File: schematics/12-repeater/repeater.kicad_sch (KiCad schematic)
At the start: 9 parts, among them J13 PSG01571, J5 RJHSE-5380, U6 PCA9600D

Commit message: Move schematics to correct folders
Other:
- title: PROJECT ROYALE INSTRUMENTATION -> PROJECT ROYALE REPEATER
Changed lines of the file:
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@@
   (paper "A4")
   (title_block
-    (title "PROJECT ROYALE INSTRUMENTATION")
-    (date "2021-11-26")
+    (title "PROJECT ROYALE REPEATER")
+    (date "2022-02-08")
     (rev "2.1")
     (company "Cambridge University Spaceflight")
@@
     (effects (font (size 1.27 1.27)) (justify right))
   )
-  (symbol (lib_id "royale:PCA9600D") (at 130.81 99.06 0)
+  (symbol (lib_id "royale:PCA9600D") (at 130.81 99.06 0) (unit 1)
     (in_bom yes) (on_board yes)
     (property "Reference" "U6" (id 0) (at 132.08 87.63 0)
@@
     (pin "8")
   )
-  (symbol (lib_id "royale:R") (at 111.76 91.44 270)
+  (symbol (lib_id "royale:R") (at 111.76 91.44 270) (unit 1)
     (in_bom yes) (on_board yes)
     (property "Reference" "R25" (id 0) (at 113.03 91.44 90)
@@
     (pin "2")
   )
-  (symbol (lib_id "royale:R") (at 104.14 91.44 270)
+  (symbol (lib_id "royale:R") (at 104.14 91.44 270) (unit 1)
     (in_bom yes) (on_board yes)
     (property "Reference" "R24" (id 0) (at 105.41 91.44 90)
@@
     (pin "2")
   )
-  (symbol (lib_id "royale:R") (at 146.05 88.9 270)
+  (symbol (lib_id "royale:R") (at 146.05 88.9 270) (unit 1)
     (in_bom yes) (on_board yes)
     (property "Reference" "R26" (id 0) (at 147.32 88.9 90)
@@
     (pin "2")
   )
-  (symbol (lib_id "royale:R") (at 161.29 88.9 270)
+  (symbol (lib_id "royale:R") (at 161.29 88.9 270) (unit 1)
     (in_bom yes) (on_board yes)
     (property "Reference" "R27" (id 0) (at 162.56 88.9 90)
@@
     (pin "2")
   )
-  (symbol (lib_id "royale:12v") (at 130.81 82.55 0)
+  (symbol (lib_id "royale:12v") (at 130.81 82.55 0) (unit 1)
     (in_bom yes) (on_board yes)
     (property "Reference" "#PWR028" (id 0) (at 130.81 79.756 0)
@@
     (pin "1")
   )
-  (symbol (lib_id "cusf-kicad:GND") (at 130.81 114.3 0)
+  (symbol (lib_id "cusf-kicad:GND") (at 130.81 114.3 0) (unit 1)
     (in_bom yes) (on_board yes)
     (property "Reference" "#PWR029" (id 0) (at 127.508 113.284 0)
@@
     (pin "1")
   )
-  (symbol (lib_id "royale:GND") (at 203.2 104.14 0)
+  (symbol (lib_id "royale:GND") (at 203.2 104.14 0) (unit 1)
     (in_bom yes) (on_board yes)
     (property "Reference" "#PWR051" (id 0) (at 199.898 103.124 0)
@@
     (pin "1")
   )
-  (symbol (lib_id "royale:GND") (at 185.42 104.14 0)
+  (symbol (lib_id "royale:GND") (at 185.42 104.14 0) (unit 1)
     (in_bom yes) (on_board yes)
     (property "Reference" "#PWR049" (id 0) (at 182.118 103.124 0)
@@
     (pin "1")
   )
-  (symbol (lib_id "royale:Conn_02x04") (at 193.04 96.52 0)
+  (symbol (lib_id "royale:Conn_02x04") (at 193.04 96.52 0) (unit 1)
     (in_bom yes) (on_board yes)
     (property "Reference" "J5" (id 0) (at 194.31 87.63 0))
@@
     (pin "8")
   )
-  (symbol (lib_id "royale:3v3") (at 104.14 82.55 0)
+  (symbol (lib_id "royale:3v3") (at 104.14 82.55 0) (unit 1)
     (in_bom yes) (on_board yes)
     (property "Reference" "#PWR027" (id 0) (at 104.14 79.756 0)
@@
     (pin "1")
   )
-  (symbol (lib_id "royale:C") (at 173.99 106.68 90) (mirror x)
+  (symbol (lib_id "royale:C") (at 173.99 106.68 90) (mirror x) (unit 1)
     (in_bom yes) (on_board yes)
     (property "Reference" "C17" (id 0) (at 172.72 106.68 90)
@@
     (pin "2")
   )
-  (symbol (lib_id "royale:12v") (at 185.42 91.44 0)
+  (symbol (lib_id "royale:12v") (at 185.42 91.44 0) (unit 1)
     (in_bom yes) (on_board yes)
     (property "Reference" "#PWR048" (id 0) (at 185.42 88.646 0)
@@
     (pin "1")
   )
-  (symbol (lib_id "royale:12v") (at 203.2 91.44 0)
+  (symbol (lib_id "royale:12v") (at 203.2 91.44 0) (unit 1)
     (in_bom yes) (on_board yes)
     (property "Reference" "#PWR050" (id 0) (at 203.2 88.646 0)
@@
     (pin "1")
   )
-  (symbol (lib_id "Diode:BAT54A") (at 151.13 106.68 0)
+  (symbol (lib_id "Diode:BAT54A") (at 151.13 106.68 0) (unit 1)
     (in_bom yes) (on_board yes) (fields_autoplaced)
     (property "Reference" "D2" (id 0) (at 151.13 100.33 0))
@@
     (pin "3")
   )
-  (symbol (lib_id "Connector:Mini-DIN-4") (at 81.28 111.76 0)
+  (symbol (lib_id "Connector:Mini-DIN-4") (at 81.28 111.76 0) (unit 1)
     (in_bom yes) (on_board yes)
     (property "Reference" "J13" (id 0) (at 88.9 105.41 0))
@@
     (pin "4")
   )
-  (symbol (lib_id "cusf-kicad:GND") (at 90.17 113.03 0)
+  (symbol (lib_id "cusf-kicad:GND") (at 90.17 113.03 0) (unit 1)
     (in_bom yes) (on_board yes)
     (property "Reference" "#PWR0103" (id 0) (at 86.868 112.014 0)
@@
     (pin "1")
   )
-  (symbol (lib_id "royale:12v") (at 73.66 115.57 180)
+  (symbol (lib_id "royale:12v") (at 73.66 115.57 180) (unit 1)
     (in_bom yes) (on_board yes)
     (property "Reference" "#PWR0104" (id 0) (at 73.66 118.364 0)
@@
     (pin "1")
   )
+  (sheet_instances
+    (path "/" (page "1"))
+  )
+  (symbol_instances
+    (path "/00000000-0000-0000-0000-000061a3f116"
+      (reference "#PWR027") (unit 1) (value "3v3") (footprint "")
+    )
+    (path "/00000000-0000-0000-0000-000061a2516b"
+      (reference "#PWR028") (unit 1) (value "12v") (footprint "")
+    )
+    (path "/00000000-0000-0000-0000-000061a2a4f9"
+      (reference "#PWR029") (unit 1) (value "GND") (footprint "")
+    )
+    (path "/00000000-0000-0000-0000-000061a8760f"
+      (reference "#PWR048") (unit 1) (value "12v") (footprint "")
+    )
+    (path "/00000000-0000-0000-0000-000061a2d2a3"
+      (reference "#PWR049") (unit 1) (value "GND") (footprint "")
+    )
+    (path "/00000000-0000-0000-0000-000061a879ee"
+      (reference "#PWR050") (unit 1) (value "12v") (footprint "")
+    )
+    (path "/00000000-0000-0000-0000-000061a2d29d"
+      (reference "#PWR051") (unit 1) (value "GND") (footprint "")
+    )
+    (path "/9d167c4c-9461-46c4-b3b1-4f3c97404f84"
+      (reference "#PWR0103") (unit 1) (value "GND") (footprint "")
+    )
+    (path "/ddaa02b0-5d92-43df-8cef-df7e364db8e9"
+      (reference "#PWR0104") (unit 1) (value "12v") (footprint "")
+    )
+    (path "/00000000-0000-0000-0000-000061a5eef5"
+      (reference "C17") (unit 1) (value "100n") (footprint "Capacitor_SMD:C_0805_2012Metric")
+    )
+    (path "/329ba30f-e553-429f-91ff-34fe3180484b"
+      (reference "D2") (unit 1) (value "BAT54A") (footprint "Package_TO_SOT_SMD:SOT-23")
+    )
+    (path "/00000000-0000-0000-0000-000061a2d2be"
+      (reference "J5") (unit 1) (value "RJHSE-5380") (footprint "Connector_RJ:RJ45_Amphenol_RJHSE5380")
+    )
+    (path "/91b1515f-01d7-467f-9976-fa4a3565e617"
+      (reference "J13") (unit 1) (value "PSG01571") (footprint "royale:Mini-Din-Through-Hole")
+    )
+    (path "/00000000-0000-0000-0000-000061a1c307"
+      (reference "R24") (unit 1) (value "4k7") (footprint "Resistor_SMD:R_0805_2012Metric")
+    )
+    (path "/00000000-0000-0000-0000-000061a1be3c"
+      (reference "R25") (unit 1) (value "4k7") (footprint "Resistor_SMD:R_0805_2012Metric")
+    )
+    (path "/00000000-0000-0000-0000-000061a1c730"
+      (reference "R26") (unit 1) (value "1k") (footprint "Resistor_SMD:R_0805_2012Metric")
+    )
+    (path "/00000000-0000-0000-0000-000061a1d18c"
+      (reference "R27") (unit 1) (value "1k") (footprint "Resistor_SMD:R_0805_2012Metric")
+    )
+    (path "/00000000-0000-0000-0000-000061a0d3e3"
+      (reference "U6") (unit 1) (value "PCA9600D") (footprint "Package_SO:SO-8_3.9x4.9mm_P1.27mm")
+    )
+  )
 )

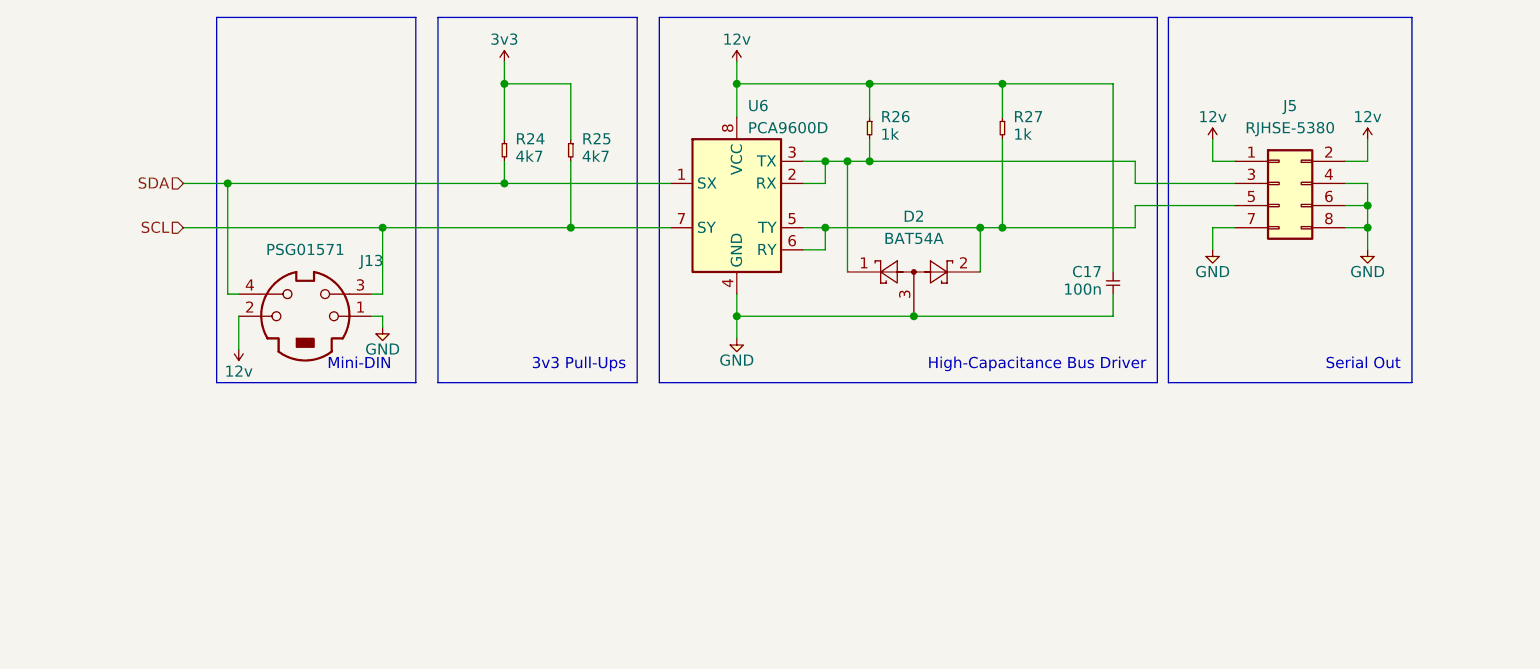
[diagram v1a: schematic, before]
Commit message: Clean up schematic and re-wire RJ45 connector
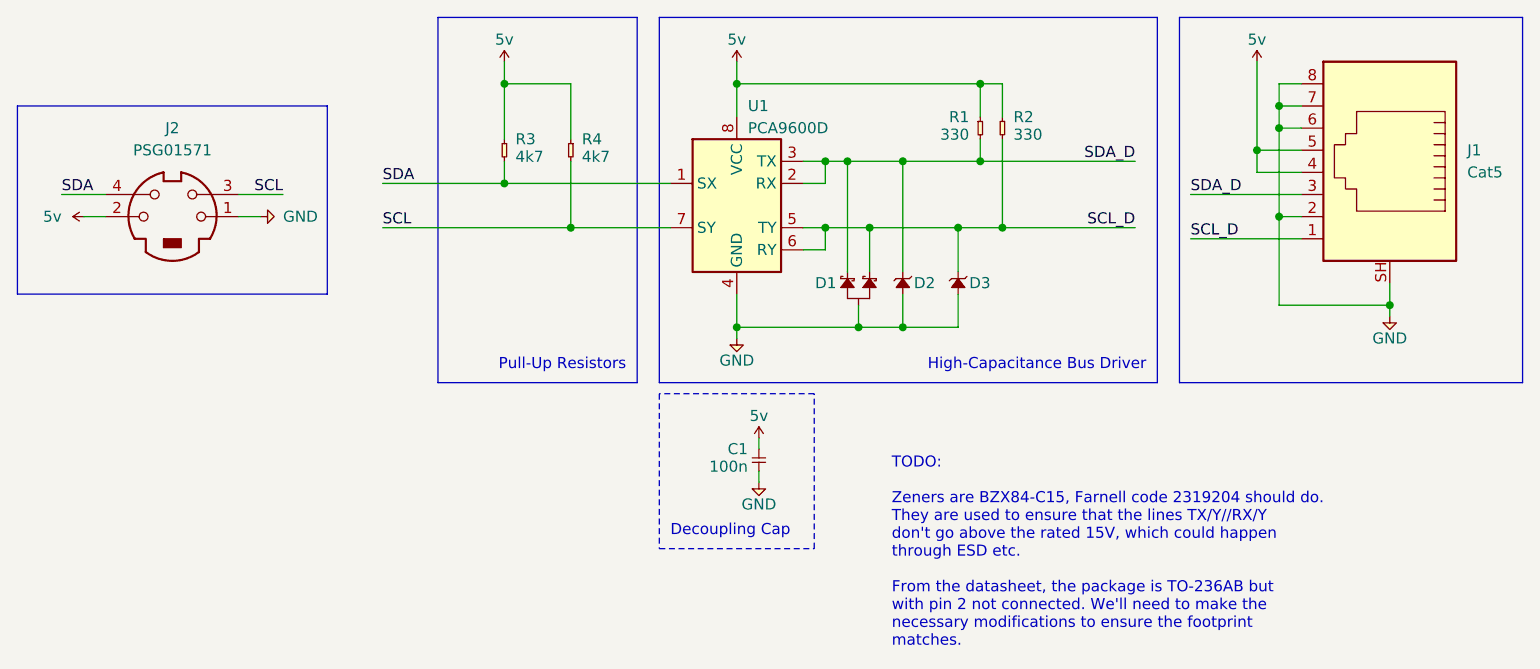
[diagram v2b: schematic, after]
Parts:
- removed D2: BAT54A, Package_TO_SOT_SMD:SOT-23, symbol Diode:BAT54A
- removed J5: RJHSE-5380, Connector_RJ:RJ45_Amphenol_RJHSE5380, symbol royale:Conn_02x04
- added D1: BAT54A, symbol royale:BAT54A
- added D2, D3: Diode_Zener, symbol royale:Diode_Zener
- added J1: Cat5, royale:RJ45_Amphenol_RJHSE5380, symbol royale:RJ45_Shielded
- R1: renamed from R26; value 1k -> 330
- R2: renamed from R27; value 1k -> 330
- renumbered C17 to C1, J13 to J2, R24 to R3, R25 to R4, U6 to U1
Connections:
- net GND: now also D1.3, D2.2, D3.2, J1.2, J1.6, J1.7, J1.8, J1.SH
- net SDA_D: now reaches R1.2, U1.2 (RX), U1.3 (TX)
- net SDA_D: now also D1.1, D2.1, J1.3
- net SCL_D: now reaches R2.2, U1.5 (TY), U1.6 (RY)
- net SCL_D: now also D1.2, D3.1, J1.1
- net 3v3 renamed 1v8
- net 1v8: now also J1.4, J1.5
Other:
- note added: "Decoupling Cap"
- note added: "Pull-Up Resistors"
- note added: "TODO: Zeners are BZX84-C15, Farnell code 2319204 should do. They are used to ensure that the lines TX/Y//RX/Y don't go above the rated 15V, which could happen through ESD etc. From the datasheet, the package is TO-236AB but with pin 2 not connected. We'll need to make the necessary modifications to ensure the footprint matches."
- note removed: "3v3 Pull-Ups"
- note removed: "Mini-DIN"
- note removed: "Serial Out"
- moved on the sheet: C1, J2, R1

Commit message: Preliminary board layout
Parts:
- D1: footprint (none) -> Package_TO_SOT_SMD:SOT-23
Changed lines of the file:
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@@
   (symbol (lib_id "royale:BAT54A") (at 143.51 106.68 90) (mirror x) (unit 1)
     (in_bom yes) (on_board yes)
-    (property "Reference" "D1" (id 0) (at 142.24 107.95 90)
+    (property "Reference" "D1" (id 0) (at 144.78 105.41 90)
       (effects (font (size 1.27 1.27)) (justify left))
     )
-    (property "Value" "BAT54A" (id 1) (at 149.86 107.95 0)
-      (effects (font (size 1.27 1.27)) hide)
-    )
-    (property "Footprint" "" (id 2) (at 144.272 105.41 0)
-      (effects (font (size 1.27 1.27)) hide)
-    )
-    (property "Datasheet" "" (id 3) (at 141.732 107.95 0)
+    (property "Value" "BAT54A" (id 1) (at 144.78 113.03 0)
+      (effects (font (size 1.27 1.27)) hide)
+    )
+    (property "Footprint" "Package_TO_SOT_SMD:SOT-23" (id 2) (at 142.24 107.442 0)
+      (effects (font (size 1.27 1.27)) hide)
+    )
+    (property "Datasheet" "" (id 3) (at 144.78 104.902 0)
       (effects (font (size 1.27 1.27)) hide)
     )
@@
     )
     (path "/1f229454-5ca3-4940-8d58-e0a83e5cb2d3"
-      (reference "D1") (unit 1) (value "BAT54A") (footprint "")
+      (reference "D1") (unit 1) (value "BAT54A") (footprint "Package_TO_SOT_SMD:SOT-23")
     )
     (path "/862d86b9-cae6-4fe1-8cc0-ad397c811d7f"

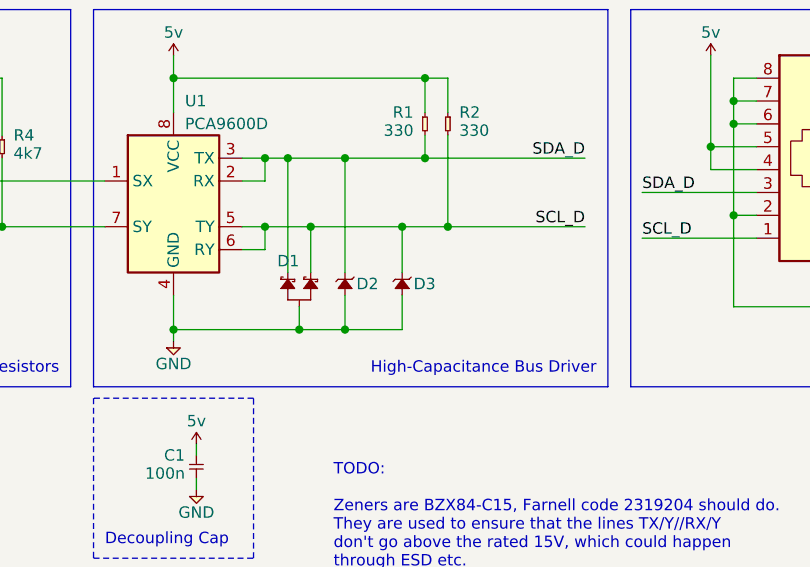
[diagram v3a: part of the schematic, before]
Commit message: added BZX84-C15 diodes, 1.8v not fixed
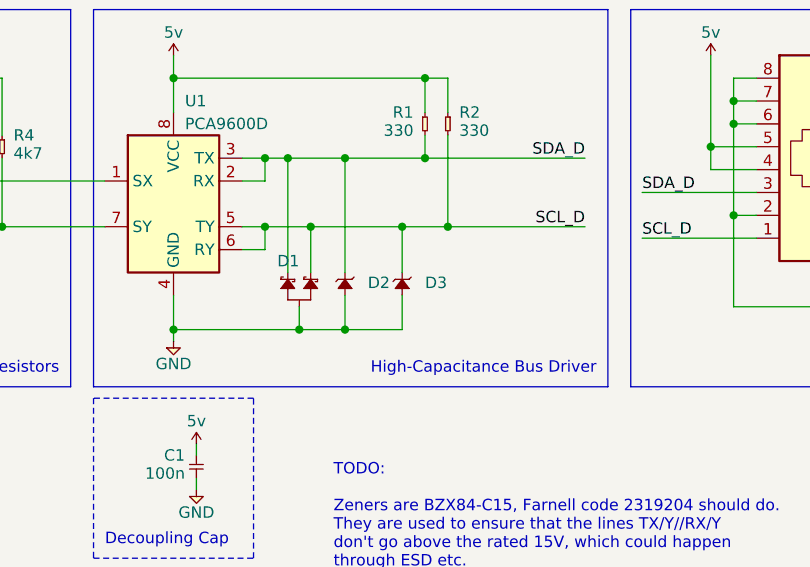
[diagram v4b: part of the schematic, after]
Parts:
- removed D2, D3: Diode_Zener, symbol royale:Diode_Zener
- added D2, D3: Diode_Zener_BZX84-C15, Package_TO_SOT_SMD:SOT-23, symbol royale:Diode_Zener_BZX84-C15
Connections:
- net GND: now also D2.1 (A), D3.1 (A)
- net SCL_D: now also D3.3 (K)
- net SDA_D: now also D2.3 (K)
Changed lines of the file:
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@@
     (pin "1")
+  )
+  (symbol (lib_id "royale:Diode_Zener_BZX84-C15") (at 156.21 106.68 270) (unit 1)
+    (in_bom yes) (on_board yes) (fields_autoplaced)
+    (property "Reference" "D3" (id 0) (at 158.75 107.8229 90)
+      (effects (font (size 1.27 1.27)) (justify left))
+    )
+    (property "Value" "Diode_Zener_BZX84-C15" (id 1) (at 154.432 107.95 0)
+      (effects (font (size 1.27 1.27)) hide)
+    )
+    (property "Footprint" "Package_TO_SOT_SMD:SOT-23" (id 2) (at 156.21 106.68 0)
+      (effects (font (size 1.27 1.27)) hide)
+    )
+    (property "Datasheet" "" (id 3) (at 156.21 106.68 0)
+      (effects (font (size 1.27 1.27)) hide)
+    )
+    (pin "1")
+    (pin "3")
   )
   (symbol (lib_id "royale:RJ45_Shielded") (at 205.74 95.25 0) (mirror y) (unit 1)
@@
     (pin "1")
   )
-  (symbol (lib_id "royale:Diode_Zener") (at 149.86 106.68 270) (unit 1)
-    (in_bom yes) (on_board yes)
-    (property "Reference" "D2" (id 0) (at 151.13 107.95 90)
+  (symbol (lib_id "royale:Diode_Zener_BZX84-C15") (at 149.86 106.68 270) (unit 1)
+    (in_bom yes) (on_board yes) (fields_autoplaced)
+    (property "Reference" "D2" (id 0) (at 152.4 107.8229 90)
       (effects (font (size 1.27 1.27)) (justify left))
     )
-    (property "Value" "Diode_Zener" (id 1) (at 148.082 107.95 0)
+    (property "Value" "Diode_Zener_BZX84-C15" (id 1) (at 148.082 107.95 0)
       (effects (font (size 1.27 1.27)) hide)
     )
-    (property "Footprint" "" (id 2) (at 149.86 106.68 0)
+    (property "Footprint" "Package_TO_SOT_SMD:SOT-23" (id 2) (at 149.86 106.68 0)
       (effects (font (size 1.27 1.27)) hide)
     )
@@
     )
     (pin "1")
-    (pin "2")
-  )
-  (symbol (lib_id "royale:Diode_Zener") (at 156.21 106.68 270) (unit 1)
-    (in_bom yes) (on_board yes)
-    (property "Reference" "D3" (id 0) (at 157.48 107.95 90)
-      (effects (font (size 1.27 1.27)) (justify left))
-    )
-    (property "Value" "Diode_Zener" (id 1) (at 154.432 107.95 0)
-      (effects (font (size 1.27 1.27)) hide)
-    )
-    (property "Footprint" "" (id 2) (at 156.21 106.68 0)
-      (effects (font (size 1.27 1.27)) hide)
-    )
-    (property "Datasheet" "" (id 3) (at 156.21 106.68 0)
-      (effects (font (size 1.27 1.27)) hide)
-    )
-    (pin "1")
-    (pin "2")
+    (pin "3")
   )
   (symbol (lib_id "Connector:Mini-DIN-4") (at 66.04 100.33 0) (unit 1)
@@
       (reference "D1") (unit 1) (value "BAT54A") (footprint "Package_TO_SOT_SMD:SOT-23")
     )
-    (path "/862d86b9-cae6-4fe1-8cc0-ad397c811d7f"
-      (reference "D2") (unit 1) (value "Diode_Zener") (footprint "")
+    (path "/7b0a639f-b224-4120-995b-ff8f50806ed0"
+      (reference "D2") (unit 1) (value "Diode_Zener_BZX84-C15") (footprint "Package_TO_SOT_SMD:SOT-23")
     )
-    (path "/8e480758-7b5c-4376-996f-9c0aba64fdbd"
-      (reference "D3") (unit 1) (value "Diode_Zener") (footprint "")
+    (path "/66c566ca-7413-4697-a118-e41aa766e32c"
+      (reference "D3") (unit 1) (value "Diode_Zener_BZX84-C15") (footprint "Package_TO_SOT_SMD:SOT-23")
     )
     (path "/7188dc85-b662-4454-b487-e52a93f86f4b"
